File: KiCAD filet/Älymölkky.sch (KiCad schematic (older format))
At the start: 45 parts, among them P0.18_TP1 Conn_01x01_Male, U1 nRF52810-QCxx, X1 32MHz Crystal, X1_C1 12pF, X1_C2 12pF, X2 32.768 kHz Crystal, X2_C11 12pF, X2_C12 12pF

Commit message: Added changes made by Pyry, antenna, copper pour and slight changes
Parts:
- added A1: ACAG0201-2450-T, ceramic_antenna_footprint:ACAG0201-2450-T, symbol Älymölkky-rescue:ACAG0201-2450-T-ceramic_antenna_library
- U1: symbol nrf52810-custom:nRF52810-QCxx -> Älymölkky-rescue:nRF52810-QCxx-nrf52810-custom
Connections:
- net ~GND is gone; now on net Earth: GND_TP1.1 (Pin_1), hupivia1.1 (Pin_1)
- net ANTENNA: now also A1.1 (input)
- net Earth: now also A1.2 (GND), A1.3 (GND2)
- no-connect marks 8 -> 7
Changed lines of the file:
@@
 $EndComp
 $Comp
-L nrf52810-custom:nRF52810-QCxx U1
+L Älymölkky-rescue:nRF52810-QCxx-nrf52810-custom U1
 U 1 1 5C5D854C
 P 5050 5050
@@
 Wire Wire Line
 	2500 4350 2950 4350
-NoConn ~ 2500 4350
 $Comp
 L Connector:Conn_01x01_Male hupivia1
@@
 	-1   0    0    1
 $EndComp
-Text Label 3750 1450 2    50   ~ 0
-~GND
-Wire Wire Line
-	3750 1450 3950 1450
+Wire Wire Line
+	3750 1450 3850 1450
 $Comp
 L Device:Polyfuse Resettable_Fuse1
@@
 	6600 5150 6600 5450
 NoConn ~ 5950 5450
+$Comp
+L Älymölkky-rescue:ACAG0201-2450-T-ceramic_antenna_library A1
+U 1 1 5C76537B
+P 1550 4500
+F 0 "A1" H 1475 4875 50  0000 C CNN
+F 1 "ACAG0201-2450-T" H 1475 4784 50  0000 C CNN
+F 2 "ceramic_antenna_footprint:ACAG0201-2450-T" H 1550 4500 50  0001 C CNN
+F 3 "" H 1550 4500 50  0001 C CNN
+	1    1550 4500
+	1    0    0    -1
+$EndComp
+Text Label 700  4650 0    50   ~ 0
+ANTENNA
+Wire Wire Line
+	700  4650 1100 4650
+$Comp
+L power:Earth #PWR0124
+U 1 1 5C76B789
+P 1950 4500
+F 0 "#PWR0124" H 1950 4250 50  0001 C CNN
+F 1 "Earth" H 1950 4350 50  0001 C CNN
+F 2 "" H 1950 4500 50  0001 C CNN
+F 3 "~" H 1950 4500 50  0001 C CNN
+	1    1950 4500
+	1    0    0    -1
+$EndComp
+Wire Wire Line
+	1950 4500 1850 4500
+$Comp
+L power:Earth #PWR0125
+U 1 1 5C771CF3
+P 1000 4350
+F 0 "#PWR0125" H 1000 4100 50  0001 C CNN
+F 1 "Earth" H 1000 4200 50  0001 C CNN
+F 2 "" H 1000 4350 50  0001 C CNN
+F 3 "~" H 1000 4350 50  0001 C CNN
+	1    1000 4350
+	1    0    0    -1
+$EndComp
+Wire Wire Line
+	1100 4350 1000 4350
+Text Label 3750 1450 2    50   ~ 0
+~GND
+$Comp
+L power:Earth #PWR?
+U 1 1 5C74A65C
+P 3850 1600
+F 0 "#PWR?" H 3850 1350 50  0001 C CNN
+F 1 "Earth" H 3850 1450 50  0001 C CNN
+F 2 "" H 3850 1600 50  0001 C CNN
+F 3 "~" H 3850 1600 50  0001 C CNN
+	1    3850 1600
+	1    0    0    -1
+$EndComp
+Wire Wire Line
+	3850 1450 3850 1600
+Connection ~ 3850 1450
+Wire Wire Line
+	3850 1450 3950 1450
 $EndSCHEMATC

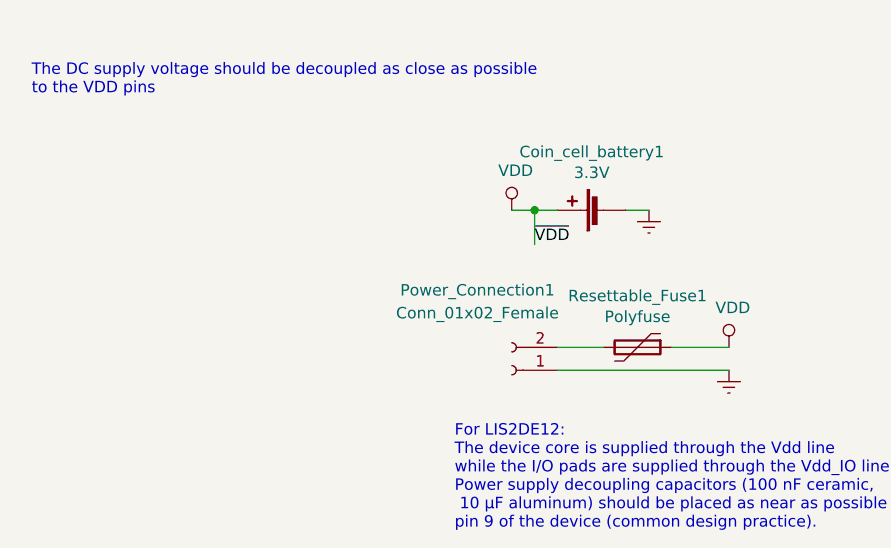
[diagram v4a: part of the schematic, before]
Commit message: Added switch, modified components to right sizes
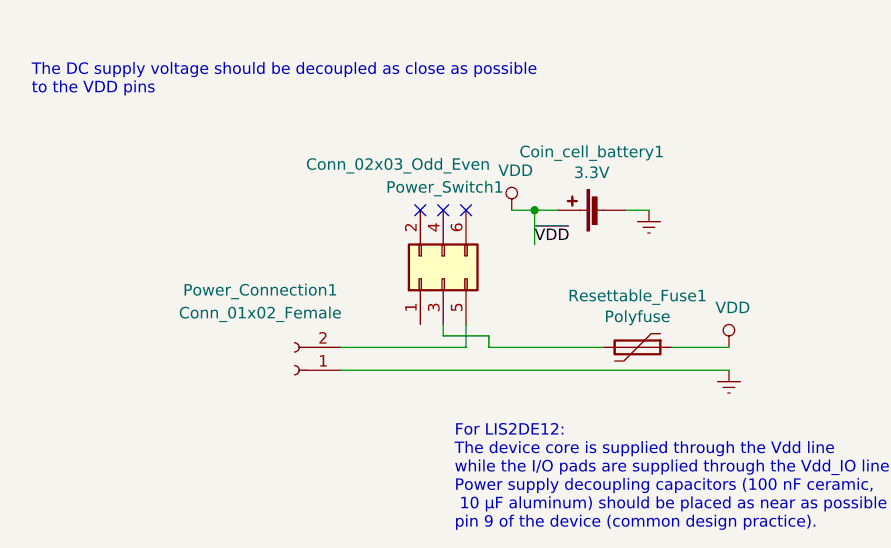
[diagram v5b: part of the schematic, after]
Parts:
- added Power_Switch1: Conn_02x03_Odd_Even, Connector_PinHeader_1.27mm:PinHeader_2x03_P1.27mm_Vertical_SMD, symbol Connector_Generic:Conn_02x03_Odd_Even
- DCC_L3: footprint Capacitor_SMD:C_0805_2012Metric_Pad1.15x1.40mm_HandSolder -> Capacitor_SMD:C_0402_1005Metric
- L1: footprint Resistor_SMD:R_0805_2012Metric_Pad1.15x1.40mm_HandSolder -> Resistor_SMD:R_0402_1005Metric
- X1_C1, X1_C2, X2_C11, X2_C12: footprint Capacitor_SMD:C_0402_1005Metric -> Capacitor_SMD:C_0805_2012Metric_Pad1.15x1.40mm_HandSolder
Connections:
- net at Power_Connection1.2 (Pin_2): now also Power_Switch1.5 (Pin_5); no longer Resettable_Fuse1.2
- new net: Power_Switch1.3 (Pin_3), Resettable_Fuse1.2
- no-connect marks 7 -> 10
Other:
- moved on the sheet: Power_Connection1
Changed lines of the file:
@@
 F 0 "L1" V 3000 4350 50  0000 L TNN
 F 1 "3.9nH" V 3200 4350 50  0000 C CNN
-F 2 "Resistor_SMD:R_0805_2012Metric_Pad1.15x1.40mm_HandSolder" H 3100 4350 50  0001 C CNN
+F 2 "Resistor_SMD:R_0402_1005Metric" H 3100 4350 50  0001 C CNN
 F 3 "~" H 3100 4350 50  0001 C CNN
 	1    3100 4350
@@
 F 0 "X1_C1" V 2248 4850 50  0000 C CNN
 F 1 "12pF" V 2339 4850 50  0000 C CNN
-F 2 "Capacitor_SMD:C_0402_1005Metric" H 2538 4700 50  0001 C CNN
+F 2 "Capacitor_SMD:C_0805_2012Metric_Pad1.15x1.40mm_HandSolder" H 2538 4700 50  0001 C CNN
 F 3 "~" H 2500 4850 50  0001 C CNN
 	1    2500 4850
@@
 F 0 "X1_C2" V 2248 5300 50  0000 C CNN
 F 1 "12pF" V 2339 5300 50  0000 C CNN
-F 2 "Capacitor_SMD:C_0402_1005Metric" H 2538 5150 50  0001 C CNN
+F 2 "Capacitor_SMD:C_0805_2012Metric_Pad1.15x1.40mm_HandSolder" H 2538 5150 50  0001 C CNN
 F 3 "~" H 2500 5300 50  0001 C CNN
 	1    2500 5300
@@
 F 0 "X2_C11" V 6298 3750 50  0000 C CNN
 F 1 "12pF" V 6389 3750 50  0000 C CNN
-F 2 "Capacitor_SMD:C_0402_1005Metric" H 6588 3600 50  0001 C CNN
+F 2 "Capacitor_SMD:C_0805_2012Metric_Pad1.15x1.40mm_HandSolder" H 6588 3600 50  0001 C CNN
 F 3 "~" H 6550 3750 50  0001 C CNN
 	1    6550 3750
@@
 F 0 "X2_C12" V 6700 4200 50  0000 C TNN
 F 1 "12pF" V 6850 4200 50  0000 C CNN
-F 2 "Capacitor_SMD:C_0402_1005Metric" H 6588 4050 50  0001 C CNN
+F 2 "Capacitor_SMD:C_0805_2012Metric_Pad1.15x1.40mm_HandSolder" H 6588 4050 50  0001 C CNN
 F 3 "~" H 6550 4200 50  0001 C CNN
 	1    6550 4200
@@
 F 0 "DCC_L3" H 4553 1846 50  0000 L CNN
 F 1 "15nH" H 4553 1755 50  0000 L CNN
-F 2 "Capacitor_SMD:C_0805_2012Metric_Pad1.15x1.40mm_HandSolder" H 4500 1800 50  0001 C CNN
+F 2 "Capacitor_SMD:C_0402_1005Metric" H 4500 1800 50  0001 C CNN
 F 3 "~" H 4500 1800 50  0001 C CNN
 	1    4500 1800
@@
 L Connector:Conn_01x02_Female Power_Connection1
 U 1 1 5C6A2D8F
-P 9200 2200
-F 0 "Power_Connection1" H 9350 1850 50  0000 C CNN
-F 1 "Conn_01x02_Female" H 9350 1950 50  0000 C CNN
-F 2 "Connector_PinHeader_2.54mm:PinHeader_1x02_P2.54mm_Vertical" H 9200 2200 50  0001 C CNN
-F 3 "~" H 9200 2200 50  0001 C CNN
-	1    9200 2200
+P 8250 2200
+F 0 "Power_Connection1" H 8400 1850 50  0000 C CNN
+F 1 "Conn_01x02_Female" H 8400 1950 50  0000 C CNN
+F 2 "Connector_PinHeader_2.54mm:PinHeader_1x02_P2.54mm_Vertical" H 8250 2200 50  0001 C CNN
+F 3 "~" H 8250 2200 50  0001 C CNN
+	1    8250 2200
 	-1   0    0    1
 $EndComp
@@
 $EndComp
 Wire Wire Line
-	9400 2100 9600 2100
-Wire Wire Line
 	9900 2100 10150 2100
-Wire Wire Line
-	9400 2200 10150 2200
 Wire Wire Line
 	7650 3350 8200 3350
@@
 ~GND
 $Comp
-L power:Earth #PWR?
+L power:Earth #PWR0126
 U 1 1 5C74A65C
 P 3850 1600
-F 0 "#PWR?" H 3850 1350 50  0001 C CNN
+F 0 "#PWR0126" H 3850 1350 50  0001 C CNN
 F 1 "Earth" H 3850 1450 50  0001 C CNN
 F 2 "" H 3850 1600 50  0001 C CNN
@@
 Wire Wire Line
 	3850 1450 3950 1450
+$Comp
+L Connector_Generic:Conn_02x03_Odd_Even Power_Switch1
+U 1 1 5C758E30
+P 8900 1800
+F 0 "Power_Switch1" V 9300 2050 50  0000 R CNN
+F 1 "Conn_02x03_Odd_Even" V 9400 2400 50  0000 R CNN
+F 2 "Connector_PinHeader_1.27mm:PinHeader_2x03_P1.27mm_Vertical_SMD" H 8900 1800 50  0001 C CNN
+F 3 "~" H 8900 1800 50  0001 C CNN
+	1    8900 1800
+	0    -1   -1   0
+$EndComp
+NoConn ~ 9000 1500
+NoConn ~ 8900 1500
+NoConn ~ 8800 1500
+Wire Wire Line
+	8450 2200 10150 2200
+Wire Wire Line
+	8450 2100 9000 2100
+Wire Wire Line
+	9000 2100 9000 2000
+Wire Wire Line
+	8900 2000 8900 2050
+Wire Wire Line
+	8900 2050 9100 2050
+Wire Wire Line
+	9100 2050 9100 2100
+Wire Wire Line
+	9100 2100 9600 2100
 $EndSCHEMATC
